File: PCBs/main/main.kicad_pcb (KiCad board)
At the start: 2 copper layers, 2 parts, among them J4 Conn_02x10_Odd_Even

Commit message: work on first prototype for the boards
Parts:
- removed A1: Arduino_Mega2560_R3_Shield, PCM_arduino-library:Arduino_Mega2560_R3_Shield
- added A2: Arduino_Mega2560_R3_Shield, PCM_arduino-library:Arduino_Mega2560_R3_Shield, F.Cu at (87.2, 90.5)
- added J1: Conn_02x05_Counter_Clockwise, Connector_IDC:IDC-Header_2x05_P2.54mm_Vertical, F.Cu at (142.7, 48.0)
- added J2: Conn_02x05_Counter_Clockwise, Connector_IDC:IDC-Header_2x05_P2.54mm_Vertical, F.Cu at (119.7, 48.0)
- added J3: Conn_02x05_Counter_Clockwise, Connector_IDC:IDC-Header_2x05_P2.54mm_Vertical, F.Cu at (171.0, 61.1)
- added J5: chambers 9-10, Connector_IDC:IDC-Header_2x05_P2.54mm_Vertical, F.Cu at (173.1, 47.7)
- J4: value Conn_02x10_Odd_Even -> Conn_02x05_Counter_Clockwise; footprint Connector_IDC:IDC-Header_2x10_P2.54mm_Vertical -> Connector_IDC:IDC-Header_2x05_P2.54mm_Vertical
- moved J4 67.8 mm to (140.2, 61.7), turned to 0 degrees
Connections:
- J4 pad 1: Net-(J4-Pin_1) -> GND
- J4 pad 10: Net-(J4-Pin_10) -> GND
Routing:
- net Net-(J4-Pin_5): track 12.3 -> 80.9 mm
- net Net-(J4-Pin_7): track 12.3 -> 70.1 mm
- net Net-(J4-Pin_10): track 54.3 -> 0.00 mm
- net Net-(J4-Pin_12): track 54.3 -> 0.00 mm
- net Net-(J4-Pin_3): track 12.3 -> 60.1 mm
- net Net-(J4-Pin_9): track 12.9 -> 59.7 mm
- net Net-(J4-Pin_2): track 8.72 -> 54.5 mm
- net Net-(J4-Pin_4): track 10.3 -> 55.0 mm
- net Net-(A2-D16/TX2): track 0.00 -> 31.2 mm
- net Net-(A2-D14/TX3): track 0.00 -> 30.4 mm
- net Net-(J3-Pin_3): track 0.00 -> 27.3 mm
- net Net-(J3-Pin_9): track 0.00 -> 24.4 mm
- net Net-(J3-Pin_5): track 0.00 -> 24.2 mm
- net Net-(J3-Pin_7): track 0.00 -> 23.9 mm
- net Net-(J3-Pin_4): track 0.00 -> 17.9 mm
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- added copper zone on B.Cu, net GND
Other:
- board outline added: 103 x 56.5 mm
- board text added: "OptoChamber main board Mega Shield Modification V0.0.1 By Andre M Chagas CERN OHL V2.0 -S-"

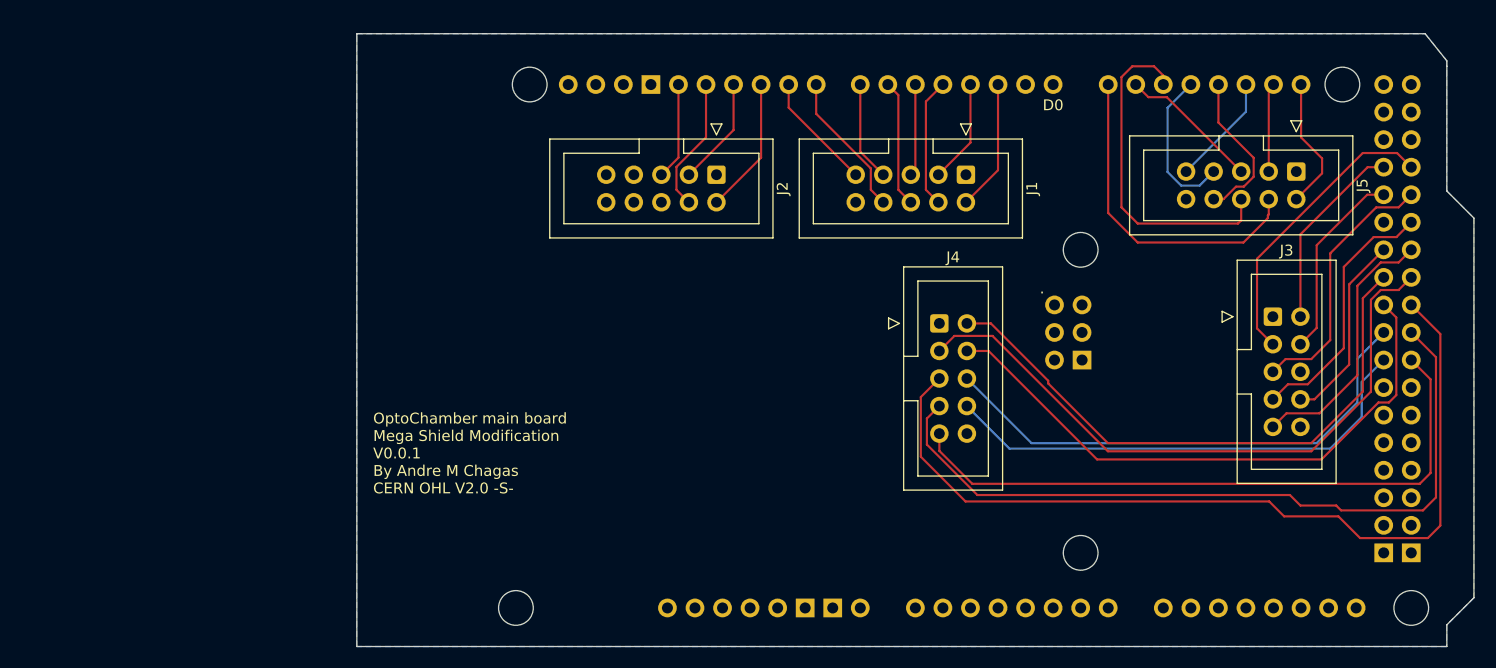
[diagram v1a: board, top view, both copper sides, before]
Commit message: update bom and finish first version of PCBs
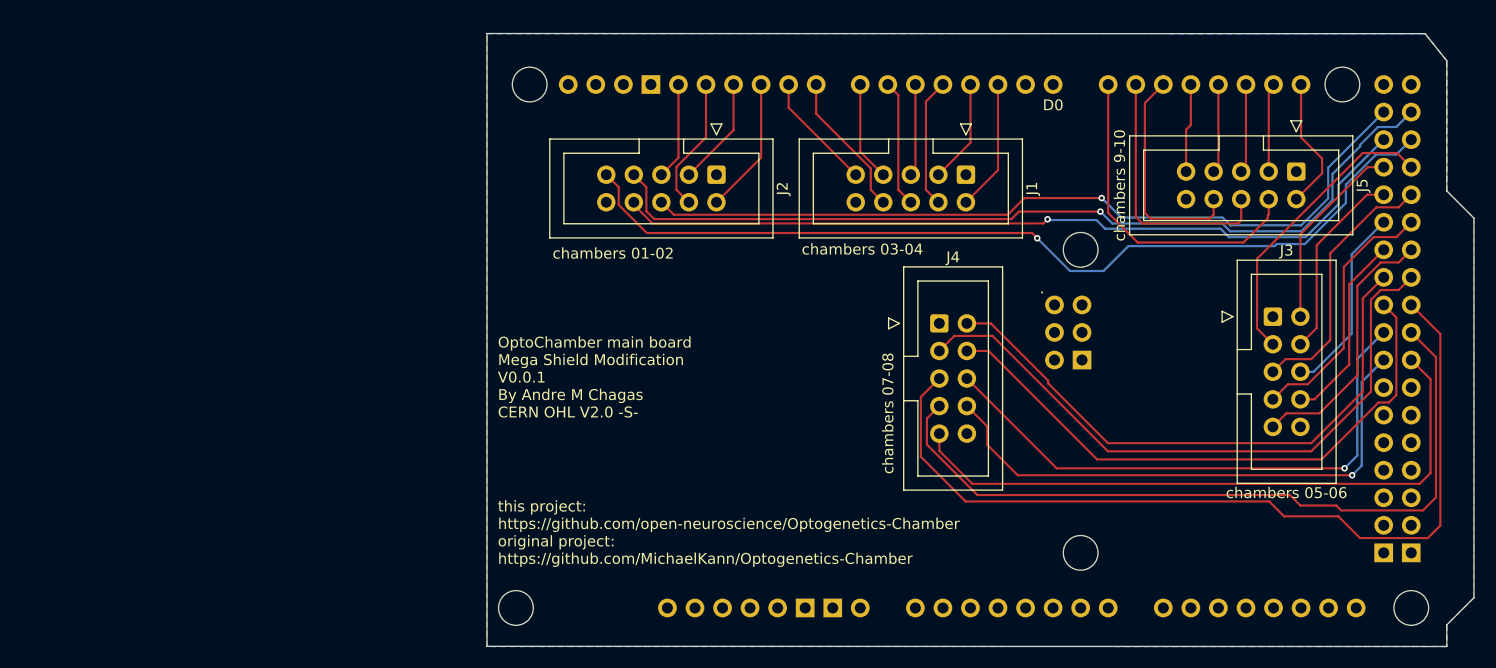
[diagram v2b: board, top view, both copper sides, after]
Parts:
- J1: value Conn_02x05_Counter_Clockwise -> chambers 03-04
- J2: value Conn_02x05_Counter_Clockwise -> chambers 01-02
- J3: value Conn_02x05_Counter_Clockwise -> chambers 05-06
- J4: value Conn_02x05_Counter_Clockwise -> chambers 07-08
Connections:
- J5 pad 5: Net-(A2-D15/RX3) -> Net-(A2-D19/RX1)
- J5 pad 6: Net-(A2-D16/TX2) -> Net-(A2-D15/RX3)
- J5 pad 7: Net-(A2-D17/RX2) -> Net-(A2-D18/TX1)
- J5 pad 8: Net-(A2-D18/TX1) -> Net-(A2-D16/TX2)
- J5 pad 9: Net-(A2-D19/RX1) -> Net-(A2-D17/RX2)
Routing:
- net Net-(J2-Pin_9): track 0.00 -> 84.9 mm, vias 0 -> 1
- net Net-(J2-Pin_7): track 0.00 -> 81.8 mm, vias 0 -> 1
- net Net-(J2-Pin_8): track 0.00 -> 75.7 mm, vias 0 -> 1
- net Net-(J2-Pin_6): track 0.00 -> 74.7 mm, vias 0 -> 1
- net Net-(J3-Pin_6): track 0.00 -> 17.7 mm
- net Net-(A2-D15/RX3): track 13.0 -> 24.2 mm
- net Net-(A2-D16/TX2): track 31.2 -> 21.5 mm
- net Net-(A2-D18/TX1): track 14.4 -> 8.21 mm
- net Net-(A2-D17/RX2): track 14.3 -> 8.21 mm
- net Net-(J4-Pin_8): track 45.3 -> 51.0 mm, vias 0 -> 1
- net Net-(J4-Pin_6): track 47.5 -> 52.3 mm, vias 0 -> 1
- net Net-(A2-D19/RX1): track 10.3 -> 8.21 mm
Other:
- board size 103 x 56.5 mm -> 91 x 56.5 mm
- board text added: "J5"
- board text added: "this project: https://github.com/open-neuroscience/Optogenetics-Chamber original project: https://github.com/MichaelKann/Optogenetics-Chamber"
